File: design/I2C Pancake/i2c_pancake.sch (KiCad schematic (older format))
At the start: 23 parts, among them J1 Conn_01x03, J2 Conn_01x03, J3 Conn_01x05_Male, J7 Conn_01x05_Male, J8 Conn_01x05_Female, Q1 2N3096, SW1 SW_DIP_x04, U2 LT1460-10, U6 PIC16F1826-ISO

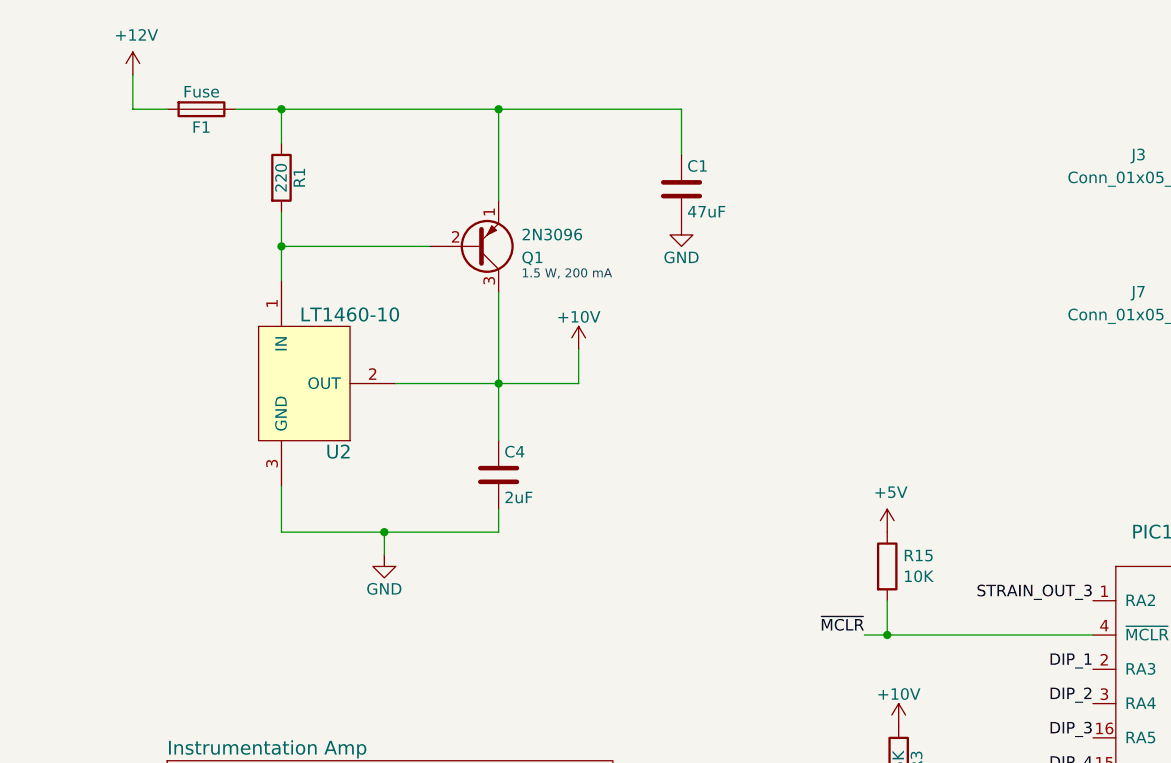
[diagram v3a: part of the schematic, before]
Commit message: Replace internal DC power supply with a Low-Dropout Regulator
The LDO regulator will convert the 12 volt input from the LiPo battery to a stable 10 volt
internal supply.
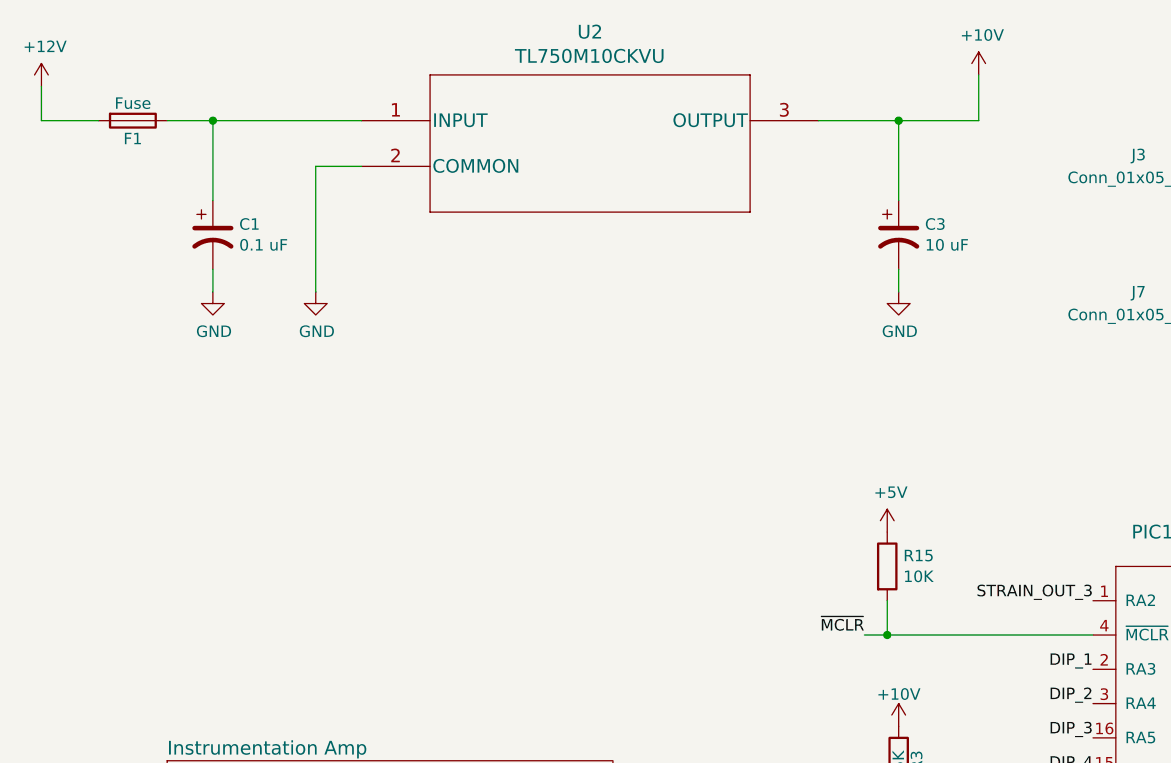
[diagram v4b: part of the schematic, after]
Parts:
- removed C1: 47uF, Capacitors_ThroughHole:CP_Radial_Tantal_D6.0mm_P2.50mm, symbol i2c_pancake-rescue:C-device
- removed C4: 2uF, Capacitors_ThroughHole:CP_Radial_Tantal_D5.0mm_P2.50mm, symbol i2c_pancake-rescue:C-device
- removed Q1: 2N3096, TO_SOT_Packages_THT:TO-92_Inline_Narrow_Oval, symbol i2c_pancake-rescue:Q_PNP_EBC-device
- removed R1: 220, Resistors_SMD:R_0805_HandSoldering, symbol i2c_pancake-rescue:R-device
- removed U2: LT1460-10, TO_SOT_Packages_THT:TO-92_Inline_Narrow_Oval, symbol i2c_pancake-rescue:LT1460-10-daq_components
- added C1: 0.1 uF, symbol Device:CP1
- added C3: 10 uF, symbol Device:CP1
- added U2: TL750M10CKVU, KVU3, symbol tlv750m10:TL750M05CKVURG3
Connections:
- net +10V: now also C3.1, U2.3 (OUTPUT)
- net GND: now also C1.2, C3.2, U2.2 (COMMON)
- net at F1.1: now also C1.1, U2.1 (INPUT)
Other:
- note removed: "1.5 W, 200 mA"
- moved on the sheet: F1
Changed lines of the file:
@@
 EESchema Schematic File Version 4
 LIBS:i2c_pancake-cache
-EELAYER 26 0
+EELAYER 30 0
 EELAYER END
 $Descr A4 11693 8268
@@
 Comment4 ""
 $EndDescr
-$Comp
-L i2c_pancake-rescue:R-device R1
-U 1 1 5ACADCA3
-P 1800 1450
-F 0 "R1" V 1880 1450 50  0000 C CNN
-F 1 "220" V 1800 1450 50  0000 C CNN
-F 2 "Resistors_SMD:R_0805_HandSoldering" V 1730 1450 50  0001 C CNN
-F 3 "" H 1800 1450 50  0000 C CNN
-	1    1800 1450
-	1    0    0    -1
-$EndComp
-$Comp
-L i2c_pancake-rescue:C-device C4
-U 1 1 5ACADCAA
-P 2750 2750
-F 0 "C4" H 2775 2850 50  0000 L CNN
-F 1 "2uF" H 2775 2650 50  0000 L CNN
-F 2 "Capacitors_ThroughHole:CP_Radial_Tantal_D5.0mm_P2.50mm" H 2788 2600 50  0001 C CNN
-F 3 "" H 2750 2750 50  0000 C CNN
-	1    2750 2750
-	1    0    0    -1
-$EndComp
-$Comp
-L power:GND #PWR01
-U 1 1 5ACADCB1
-P 2250 3100
-F 0 "#PWR01" H 2250 2850 50  0001 C CNN
-F 1 "GND" H 2250 2950 50  0000 C CNN
-F 2 "" H 2250 3100 50  0000 C CNN
-F 3 "" H 2250 3100 50  0000 C CNN
-	1    2250 3100
-	1    0    0    -1
-$EndComp
-$Comp
-L i2c_pancake-rescue:C-device C1
-U 1 1 5ACADCB7
-P 3550 1500
-F 0 "C1" H 3575 1600 50  0000 L CNN
-F 1 "47uF" H 3575 1400 50  0000 L CNN
-F 2 "Capacitors_ThroughHole:CP_Radial_Tantal_D6.0mm_P2.50mm" H 3588 1350 50  0001 C CNN
-F 3 "" H 3550 1500 50  0000 C CNN
-	1    3550 1500
-	1    0    0    -1
-$EndComp
-$Comp
-L power:GND #PWR02
-U 1 1 5ACADCBE
-P 3550 1650
-F 0 "#PWR02" H 3550 1400 50  0001 C CNN
-F 1 "GND" H 3550 1500 50  0000 C CNN
-F 2 "" H 3550 1650 50  0000 C CNN
-F 3 "" H 3550 1650 50  0000 C CNN
-	1    3550 1650
-	1    0    0    -1
-$EndComp
-$Comp
-L power:+10V #PWR03
-U 1 1 5ACADCC4
-P 3100 2200
-F 0 "#PWR03" H 3100 2050 50  0001 C CNN
-F 1 "+10V" H 3100 2340 50  0000 C CNN
-F 2 "" H 3100 2200 50  0000 C CNN
-F 3 "" H 3100 2200 50  0000 C CNN
-	1    3100 2200
-	1    0    0    -1
-$EndComp
-$Comp
-L i2c_pancake-rescue:LT1460-10-daq_components U2
-U 1 1 5ACADCDD
-P 1800 2300
-F 0 "U2" H 2050 1950 60  0000 C CNN
-F 1 "LT1460-10" H 2100 2550 60  0000 C CNN
-F 2 "TO_SOT_Packages_THT:TO-92_Inline_Narrow_Oval" H 1800 2300 60  0001 C CNN
-F 3 "" H 1800 2300 60  0001 C CNN
-	1    1800 2300
-	1    0    0    -1
-$EndComp
-$Comp
-L i2c_pancake-rescue:Q_PNP_EBC-device Q1
-U 1 1 5ACADCE4
-P 2650 1750
-F 0 "Q1" H 2850 1800 50  0000 L CNN
-F 1 "2N3096" H 2850 1700 50  0000 L CNN
-F 2 "TO_SOT_Packages_THT:TO-92_Inline_Narrow_Oval" H 2850 1850 50  0001 C CNN
-F 3 "" H 2650 1750 50  0001 C CNN
-	1    2650 1750
-	1    0    0    1
-$EndComp
-Text Notes 2850 1900 0    39   ~ 0
-1.5 W, 200 mA
 $Comp
 L i2c_pancake-rescue:Conn_01x03-strain_gauges_rtr-rescue J1
@@
 STRAIN_OUT_2
 Wire Wire Line
-	1600 1150 1800 1150
-Wire Wire Line
-	1800 1150 1800 1300
-Wire Wire Line
-	2450 1750 1800 1750
-Connection ~ 1800 1750
-Wire Wire Line
-	2750 1950 2750 2350
-Wire Wire Line
-	2300 2350 2750 2350
-Connection ~ 2750 2350
-Connection ~ 1800 1150
-Wire Wire Line
-	1800 1600 1800 1750
-Connection ~ 2750 1150
-Wire Wire Line
-	3550 1150 3550 1350
-Wire Wire Line
-	1800 2800 1800 3000
-Wire Wire Line
-	2750 1150 2750 1550
-Wire Wire Line
-	1800 3000 2250 3000
-Wire Wire Line
-	2250 3100 2250 3000
-Connection ~ 2250 3000
-Wire Wire Line
-	2750 3000 2750 2900
-Wire Wire Line
 	9600 1100 9600 1300
 Wire Wire Line
@@
 Wire Wire Line
 	3500 5850 3250 5850
-Wire Wire Line
-	3100 2350 3100 2200
 $Comp
 L i2c_pancake-rescue:Fuse-device F1
 U 1 1 5ACB8796
-P 1450 1150
-F 0 "F1" V 1530 1150 50  0000 C CNN
-F 1 "Fuse" V 1375 1150 50  0000 C CNN
-F 2 "Fuse:Fuse_1206_3216Metric_Pad1.24x1.80mm_HandSolder" V 1380 1150 50  0001 C CNN
-F 3 "" H 1450 1150 50  0001 C CNN
-	1    1450 1150
+P 1150 1200
+F 0 "F1" V 1230 1200 50  0000 C CNN
+F 1 "Fuse" V 1075 1200 50  0000 C CNN
+F 2 "Fuse:Fuse_1206_3216Metric_Pad1.24x1.80mm_HandSolder" V 1080 1200 50  0001 C CNN
+F 3 "" H 1150 1200 50  0001 C CNN
+	1    1150 1200
 	0    1    1    0
 $EndComp
-Wire Wire Line
-	1800 1750 1800 1900
-Wire Wire Line
-	2750 2350 2750 2600
-Wire Wire Line
-	2750 2350 3100 2350
-Wire Wire Line
-	2750 1150 3550 1150
-Wire Wire Line
-	2250 3000 2750 3000
 $Comp
 L Switch:SW_DIP_x04 SW1
@@
 	1    0    0    -1
 $EndComp
-Wire Wire Line
-	1800 1150 2750 1150
 $Sheet
 S 4350 5550 1950 1250
@@
 	6500 1050 6500 1750
 $Comp
-L power:GND #PWR?
+L power:GND #PWR017
 U 1 1 5EA9B7AB
 P 6900 2450
-F 0 "#PWR?" H 6900 2200 50  0001 C CNN
+F 0 "#PWR017" H 6900 2200 50  0001 C CNN
 F 1 "GND" H 6905 2277 50  0000 C CNN
 F 2 "" H 6900 2450 50  0001 C CNN
@@
 Connection ~ 4450 3450
 $Comp
-L power:+12V #PWR?
+L power:+12V #PWR01
 U 1 1 5EAED0B5
-P 1150 1000
-F 0 "#PWR?" H 1150 850 50  0001 C CNN
-F 1 "+12V" H 1165 1173 50  0000 C CNN
-F 2 "" H 1150 1000 50  0001 C CNN
-F 3 "" H 1150 1000 50  0001 C CNN
-	1    1150 1000
-	1    0    0    -1
-$EndComp
-Wire Wire Line
-	1150 1000 1150 1150
-Wire Wire Line
-	1150 1150 1300 1150
+P 750 1050
+F 0 "#PWR01" H 750 900 50  0001 C CNN
+F 1 "+12V" H 765 1223 50  0000 C CNN
+F 2 "" H 750 1050 50  0001 C CNN
+F 3 "" H 750 1050 50  0001 C CNN
+	1    750  1050
+	1    0    0    -1
+$EndComp
+Wire Wire Line
+	750  1050 750  1200
+$Comp
+L tlv750m10:TL750M05CKVURG3 U2
+U 1 1 5EAA14FA
+P 2150 1200
+F 0 "U2" H 3150 1587 60  0000 C CNN
+F 1 "TL750M10CKVU" H 3150 1481 60  0000 C CNN
+F 2 "KVU3" H 3150 1440 60  0001 C CNN
+F 3 "http://www.ti.com/lit/ds/symlink/tl750m.pdf?ts=1588185394744" H 3150 1481 60  0001 C CNN
+	1    2150 1200
+	1    0    0    -1
+$EndComp
+$Comp
+L power:GND #PWR03
+U 1 1 5EAA7F83
+P 1950 1950
+F 0 "#PWR03" H 1950 1700 50  0001 C CNN
+F 1 "GND" H 1955 1777 50  0000 C CNN
+F 2 "" H 1950 1950 50  0001 C CNN
+F 3 "" H 1950 1950 50  0001 C CNN
+	1    1950 1950
+	1    0    0    -1
+$EndComp
+$Comp
+L power:GND #PWR02
+U 1 1 5EAA88AD
+P 1500 1950
+F 0 "#PWR02" H 1500 1700 50  0001 C CNN
+F 1 "GND" H 1505 1777 50  0000 C CNN
+F 2 "" H 1500 1950 50  0001 C CNN
+F 3 "" H 1500 1950 50  0001 C CNN
+	1    1500 1950
+	1    0    0    -1
+$EndComp
+$Comp
+L power:GND #PWR04
+U 1 1 5EAA8E28
+P 4500 1950
+F 0 "#PWR04" H 4500 1700 50  0001 C CNN
+F 1 "GND" H 4505 1777 50  0000 C CNN
+F 2 "" H 4500 1950 50  0001 C CNN
+F 3 "" H 4500 1950 50  0001 C CNN
+	1    4500 1950
+	1    0    0    -1
+$EndComp
+$Comp
+L Device:CP1 C1
+U 1 1 5EAAE718
+P 1500 1700
+F 0 "C1" H 1615 1746 50  0000 L CNN
+F 1 "0.1 uF" H 1615 1655 50  0000 L CNN
+F 2 "" H 1500 1700 50  0001 C CNN
+F 3 "~" H 1500 1700 50  0001 C CNN
+	1    1500 1700
+	1    0    0    -1
+$EndComp
+$Comp
+L Device:CP1 C3
+U 1 1 5EAAF20A
+P 4500 1700
+F 0 "C3" H 4615 1746 50  0000 L CNN
+F 1 "10 uF" H 4615 1655 50  0000 L CNN
+F 2 "" H 4500 1700 50  0001 C CNN
+F 3 "~" H 4500 1700 50  0001 C CNN
+	1    4500 1700
+	1    0    0    -1
+$EndComp
+Wire Wire Line
+	750  1200 1000 1200
+Wire Wire Line
+	1300 1200 1500 1200
+Wire Wire Line
+	1500 1550 1500 1200
+Connection ~ 1500 1200
+Wire Wire Line
+	1500 1200 2150 1200
+Wire Wire Line
+	1500 1850 1500 1950
+Wire Wire Line
+	1950 1400 1950 1950
+Wire Wire Line
+	1950 1400 2150 1400
+Wire Wire Line
+	4500 1850 4500 1950
+Wire Wire Line
+	4150 1200 4500 1200
+Wire Wire Line
+	4500 1200 4500 1550
+$Comp
+L power:+10V #PWR016
+U 1 1 5EAD0FFF
+P 4850 1000
+F 0 "#PWR016" H 4850 850 50  0001 C CNN
+F 1 "+10V" H 4865 1173 50  0000 C CNN
+F 2 "" H 4850 1000 50  0001 C CNN
+F 3 "" H 4850 1000 50  0001 C CNN
+	1    4850 1000
+	1    0    0    -1
+$EndComp
+Wire Wire Line
+	4500 1200 4850 1200
+Wire Wire Line
+	4850 1200 4850 1000
+Connection ~ 4500 1200
 $EndSCHEMATC

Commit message: Update component footprints to prepare for PCB Layout update
The footprints of many components in the I2C Pancake Board
design have been updated to prepare for a new PCB Layout.
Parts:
- C1, C8: footprint (none) -> footprints:C_0805_HandSoldering
- J8: footprint (none) -> footprints:PinHeader_5x2.54_SMD_90deg_952-3198-1-ND
- R12, R13, R14, R16: footprint (none) -> footprints:R_0805_HandSoldering
- SW1: footprint (none) -> footprints:DIP_SWITCH_4X2
- U2: footprint KVU3 -> footprints:TL750M10CKVU
- U6: footprint (none) -> custom:PIC16F1826-ISO
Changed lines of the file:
@@
 F 0 "SW1" H 8550 6167 50  0000 C CNN
 F 1 "SW_DIP_x04" H 8550 6076 50  0000 C CNN
-F 2 "" H 8550 5700 50  0001 C CNN
+F 2 "footprints:DIP_SWITCH_4X2" H 8550 5700 50  0001 C CNN
 F 3 "~" H 8550 5700 50  0001 C CNN
 	1    8550 5700
@@
 F 0 "R12" H 8920 5396 50  0000 L CNN
 F 1 "10K" H 8920 5305 50  0000 L CNN
-F 2 "" V 8780 5350 50  0001 C CNN
+F 2 "footprints:R_0805_HandSoldering" V 8780 5350 50  0001 C CNN
 F 3 "~" H 8850 5350 50  0001 C CNN
 	1    8850 5350
@@
 F 0 "R13" H 9370 5396 50  0000 L CNN
 F 1 "10K" H 9370 5305 50  0000 L CNN
-F 2 "" V 9230 5350 50  0001 C CNN
+F 2 "footprints:R_0805_HandSoldering" V 9230 5350 50  0001 C CNN
 F 3 "~" H 9300 5350 50  0001 C CNN
 	1    9300 5350
@@
 F 0 "R14" H 9820 5396 50  0000 L CNN
 F 1 "10K" H 9820 5305 50  0000 L CNN
-F 2 "" V 9680 5350 50  0001 C CNN
+F 2 "footprints:R_0805_HandSoldering" V 9680 5350 50  0001 C CNN
 F 3 "~" H 9750 5350 50  0001 C CNN
 	1    9750 5350
@@
 F 0 "R16" H 10220 5396 50  0000 L CNN
 F 1 "10K" H 10220 5305 50  0000 L CNN
-F 2 "" V 10080 5350 50  0001 C CNN
+F 2 "footprints:R_0805_HandSoldering" V 10080 5350 50  0001 C CNN
 F 3 "~" H 10150 5350 50  0001 C CNN
 	1    10150 5350
@@
 F 0 "J8" H 9092 3325 50  0000 C CNN
 F 1 "Conn_01x05_Female" H 9092 3416 50  0000 C CNN
-F 2 "" H 9200 3750 50  0001 C CNN
+F 2 "footprints:PinHeader_5x2.54_SMD_90deg_952-3198-1-ND" H 9200 3750 50  0001 C CNN
 F 3 "~" H 9200 3750 50  0001 C CNN
 	1    9200 3750
@@
 F 0 "U6" H 5850 4000 60  0000 C CNN
 F 1 "PIC16F1826-ISO" H 5850 4100 60  0000 C CNN
-F 2 "" H 5850 4000 60  0001 C CNN
+F 2 "custom:PIC16F1826-ISO" H 5850 4000 60  0001 C CNN
 F 3 "" H 5850 4000 60  0001 C CNN
 	1    5850 3550
@@
 F 0 "C8" V 6648 4600 50  0000 C CNN
 F 1 "0.1uF" V 6739 4600 50  0000 C CNN
-F 2 "" H 6938 4450 50  0001 C CNN
+F 2 "footprints:C_0805_HandSoldering" H 6938 4450 50  0001 C CNN
 F 3 "~" H 6900 4600 50  0001 C CNN
 	1    6900 4600
@@
 F 0 "U2" H 3150 1587 60  0000 C CNN
 F 1 "TL750M10CKVU" H 3150 1481 60  0000 C CNN
-F 2 "KVU3" H 3150 1440 60  0001 C CNN
+F 2 "footprints:TL750M10CKVU" H 3150 1440 60  0001 C CNN
 F 3 "http://www.ti.com/lit/ds/symlink/tl750m.pdf?ts=1588185394744" H 3150 1481 60  0001 C CNN
 	1    2150 1200
@@
 F 0 "C1" H 1615 1746 50  0000 L CNN
 F 1 "0.1 uF" H 1615 1655 50  0000 L CNN
-F 2 "" H 1500 1700 50  0001 C CNN
+F 2 "footprints:C_0805_HandSoldering" H 1500 1700 50  0001 C CNN
 F 3 "~" H 1500 1700 50  0001 C CNN
 	1    1500 1700

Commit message: Add footprints to all schematic symbols
All schematic symbols have been assigned footprints.
PCB dimensions have been set, and most of the components have
been placed.
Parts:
- C3: footprint (none) -> Capacitor_THT:C_Disc_D5.0mm_W2.5mm_P2.50mm
- D1: footprint (none) -> Diode_SMD:D_MicroMELF_Hadsoldering
- F1: footprint Fuse:Fuse_1206_3216Metric_Pad1.24x1.80mm_HandSolder -> custom:littlefuse_01000020Z
- J1, J2: footprint Connectors_Phoenix:PhoenixContact_MCV-G_03x3.50mm_Vertical -> Connector_Phoenix_MC:PhoenixContact_MCV_1,5_3-G-3.5_1x03_P3.50mm_Vertical
- J3, J7: footprint (none) -> Connector_JST:JST_EH_S5B-EH_1x05_P2.50mm_Horizontal
- R15: footprint (none) -> footprints:R_0805_HandSoldering
- R17: footprint Resistor_SMD:R_0805_2012Metric_Pad1.15x1.40mm_HandSolder -> footprints:R_0805_HandSoldering
- R3, R5: footprint Resistors_SMD:R_0805_HandSoldering -> footprints:R_0805_HandSoldering
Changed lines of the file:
@@
 F 0 "J1" H 9100 1600 50  0000 C CNN
 F 1 "Conn_01x03" V 9200 1400 50  0000 C CNN
-F 2 "Connectors_Phoenix:PhoenixContact_MCV-G_03x3.50mm_Vertical" H 9100 1400 50  0001 C CNN
+F 2 "Connector_Phoenix_MC:PhoenixContact_MCV_1,5_3-G-3.5_1x03_P3.50mm_Vertical" H 9100 1400 50  0001 C CNN
 F 3 "" H 9100 1400 50  0001 C CNN
 	1    9100 1400
@@
 F 0 "J2" H 9100 2450 50  0000 C CNN
 F 1 "Conn_01x03" V 9200 2250 50  0000 C CNN
-F 2 "Connectors_Phoenix:PhoenixContact_MCV-G_03x3.50mm_Vertical" H 9100 2250 50  0001 C CNN
+F 2 "Connector_Phoenix_MC:PhoenixContact_MCV_1,5_3-G-3.5_1x03_P3.50mm_Vertical" H 9100 2250 50  0001 C CNN
 F 3 "" H 9100 2250 50  0001 C CNN
 	1    9100 2250
@@
 F 0 "R3" V 4580 4000 50  0000 C CNN
 F 1 "5K" V 4500 4000 50  0000 C CNN
-F 2 "Resistors_SMD:R_0805_HandSoldering" H 4500 4000 50  0001 C CNN
+F 2 "footprints:R_0805_HandSoldering" H 4500 4000 50  0001 C CNN
 F 3 "" H 4500 4000 50  0001 C CNN
 	1    4500 4000
@@
 F 0 "R5" V 4580 4350 50  0000 C CNN
 F 1 "10K" V 4500 4350 50  0000 C CNN
-F 2 "Resistors_SMD:R_0805_HandSoldering" H 4500 4350 50  0001 C CNN
+F 2 "footprints:R_0805_HandSoldering" H 4500 4350 50  0001 C CNN
 F 3 "" H 4500 4350 50  0001 C CNN
 	1    4500 4350
@@
 F 0 "F1" V 1230 1200 50  0000 C CNN
 F 1 "Fuse" V 1075 1200 50  0000 C CNN
-F 2 "Fuse:Fuse_1206_3216Metric_Pad1.24x1.80mm_HandSolder" V 1080 1200 50  0001 C CNN
+F 2 "custom:littlefuse_01000020Z" V 1080 1200 50  0001 C CNN
 F 3 "" H 1150 1200 50  0001 C CNN
 	1    1150 1200
@@
 F 0 "J3" H 5550 1750 50  0000 C CNN
 F 1 "Conn_01x05_Male" H 5550 1650 50  0000 C CNN
-F 2 "" H 5900 1550 50  0001 C CNN
+F 2 "Connector_JST:JST_EH_S5B-EH_1x05_P2.50mm_Horizontal" H 5900 1550 50  0001 C CNN
 F 3 "~" H 5900 1550 50  0001 C CNN
 	1    5900 1550
@@
 F 0 "J7" H 5550 2150 50  0000 C CNN
 F 1 "Conn_01x05_Male" H 5550 2050 50  0000 C CNN
-F 2 "" H 5900 2050 50  0001 C CNN
+F 2 "Connector_JST:JST_EH_S5B-EH_1x05_P2.50mm_Horizontal" H 5900 2050 50  0001 C CNN
 F 3 "~" H 5900 2050 50  0001 C CNN
 	1    5900 2050
@@
 F 0 "R15" H 4520 3196 50  0000 L CNN
 F 1 "10K" H 4520 3105 50  0000 L CNN
-F 2 "" V 4380 3150 50  0001 C CNN
+F 2 "footprints:R_0805_HandSoldering" V 4380 3150 50  0001 C CNN
 F 3 "~" H 4450 3150 50  0001 C CNN
 	1    4450 3150
@@
 F 0 "R17" H 7470 4596 50  0000 L CNN
 F 1 "330" H 7470 4505 50  0000 L CNN
-F 2 "Resistor_SMD:R_0805_2012Metric_Pad1.15x1.40mm_HandSolder" V 7330 4550 50  0001 C CNN
+F 2 "footprints:R_0805_HandSoldering" V 7330 4550 50  0001 C CNN
 F 3 "~" H 7400 4550 50  0001 C CNN
 	1    7400 4550
@@
 F 0 "D1" V 7439 4033 50  0000 R CNN
 F 1 "LED" V 7348 4033 50  0000 R CNN
-F 2 "" H 7400 4150 50  0001 C CNN
+F 2 "Diode_SMD:D_MicroMELF_Hadsoldering" H 7400 4150 50  0001 C CNN
 F 3 "~" H 7400 4150 50  0001 C CNN
 	1    7400 4150
@@
 F 0 "C3" H 4615 1746 50  0000 L CNN
 F 1 "10 uF" H 4615 1655 50  0000 L CNN
-F 2 "" H 4500 1700 50  0001 C CNN
+F 2 "Capacitor_THT:C_Disc_D5.0mm_W2.5mm_P2.50mm" H 4500 1700 50  0001 C CNN
 F 3 "~" H 4500 1700 50  0001 C CNN
 	1    4500 1700

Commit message: Improve Layout of Passive Components on the Pancake Board
-Fuse has been replaced with a 1206 polyfuse
-passive components have been rearranged in a more logical manner
-DRC rules have been imported from the RLCS v2 project
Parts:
- D1: footprint Diode_SMD:D_MicroMELF_Hadsoldering -> LED_SMD:LED_1206_3216Metric_Pad1.42x1.75mm_HandSolder
- J1, J2: footprint Connector_Phoenix_MC:PhoenixContact_MCV_1,5_3-G-3.5_1x03_P3.50mm_Vertical -> TerminalBlock_Phoenix:TerminalBlock_Phoenix_MKDS-1,5-3_1x03_P5.00mm_Horizontal
- J3, J7: footprint Connector_JST:JST_EH_S5B-EH_1x05_P2.50mm_Horizontal -> Connector_JST:JST_XH_S5B-XH-A-1_1x05_P2.50mm_Horizontal
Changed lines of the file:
@@
 F 0 "J1" H 9100 1600 50  0000 C CNN
 F 1 "Conn_01x03" V 9200 1400 50  0000 C CNN
-F 2 "Connector_Phoenix_MC:PhoenixContact_MCV_1,5_3-G-3.5_1x03_P3.50mm_Vertical" H 9100 1400 50  0001 C CNN
+F 2 "TerminalBlock_Phoenix:TerminalBlock_Phoenix_MKDS-1,5-3_1x03_P5.00mm_Horizontal" H 9100 1400 50  0001 C CNN
 F 3 "" H 9100 1400 50  0001 C CNN
 	1    9100 1400
@@
 F 0 "J2" H 9100 2450 50  0000 C CNN
 F 1 "Conn_01x03" V 9200 2250 50  0000 C CNN
-F 2 "Connector_Phoenix_MC:PhoenixContact_MCV_1,5_3-G-3.5_1x03_P3.50mm_Vertical" H 9100 2250 50  0001 C CNN
+F 2 "TerminalBlock_Phoenix:TerminalBlock_Phoenix_MKDS-1,5-3_1x03_P5.00mm_Horizontal" H 9100 2250 50  0001 C CNN
 F 3 "" H 9100 2250 50  0001 C CNN
 	1    9100 2250
@@
 F 0 "J3" H 5550 1750 50  0000 C CNN
 F 1 "Conn_01x05_Male" H 5550 1650 50  0000 C CNN
-F 2 "Connector_JST:JST_EH_S5B-EH_1x05_P2.50mm_Horizontal" H 5900 1550 50  0001 C CNN
+F 2 "Connector_JST:JST_XH_S5B-XH-A-1_1x05_P2.50mm_Horizontal" H 5900 1550 50  0001 C CNN
 F 3 "~" H 5900 1550 50  0001 C CNN
 	1    5900 1550
@@
 F 0 "J7" H 5550 2150 50  0000 C CNN
 F 1 "Conn_01x05_Male" H 5550 2050 50  0000 C CNN
-F 2 "Connector_JST:JST_EH_S5B-EH_1x05_P2.50mm_Horizontal" H 5900 2050 50  0001 C CNN
+F 2 "Connector_JST:JST_XH_S5B-XH-A-1_1x05_P2.50mm_Horizontal" H 5900 2050 50  0001 C CNN
 F 3 "~" H 5900 2050 50  0001 C CNN
 	1    5900 2050
@@
 F 0 "D1" V 7439 4033 50  0000 R CNN
 F 1 "LED" V 7348 4033 50  0000 R CNN
-F 2 "Diode_SMD:D_MicroMELF_Hadsoldering" H 7400 4150 50  0001 C CNN
+F 2 "LED_SMD:LED_1206_3216Metric_Pad1.42x1.75mm_HandSolder" H 7400 4150 50  0001 C CNN
 F 3 "~" H 7400 4150 50  0001 C CNN
 	1    7400 4150

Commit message: Add pinout labels to connectors
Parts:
- C3: footprint Capacitor_THT:C_Disc_D5.0mm_W2.5mm_P2.50mm -> footprints:C_0805_HandSoldering
- F1: footprint custom:littlefuse_01000020Z -> Fuse:Fuse_1206_3216Metric_Pad1.42x1.75mm_HandSolder
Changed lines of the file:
@@
 F 0 "F1" V 1230 1200 50  0000 C CNN
 F 1 "Fuse" V 1075 1200 50  0000 C CNN
-F 2 "custom:littlefuse_01000020Z" V 1080 1200 50  0001 C CNN
+F 2 "Fuse:Fuse_1206_3216Metric_Pad1.42x1.75mm_HandSolder" V 1080 1200 50  0001 C CNN
 F 3 "" H 1150 1200 50  0001 C CNN
 	1    1150 1200
@@
 F 0 "C3" H 4615 1746 50  0000 L CNN
 F 1 "10 uF" H 4615 1655 50  0000 L CNN
-F 2 "Capacitor_THT:C_Disc_D5.0mm_W2.5mm_P2.50mm" H 4500 1700 50  0001 C CNN
+F 2 "footprints:C_0805_HandSoldering" H 4500 1700 50  0001 C CNN
 F 3 "~" H 4500 1700 50  0001 C CNN
 	1    4500 1700
